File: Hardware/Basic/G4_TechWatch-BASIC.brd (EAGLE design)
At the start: 38 x 38 mm, 51 parts, among them J1 FTDI_DEVICESMD, SW3 SWITCH.MOM, SW4 SWITCH.MOM, SW5 SWITCH.MOM, U1 NRF52832_MODULE_MDBT42, U2 PCF8523

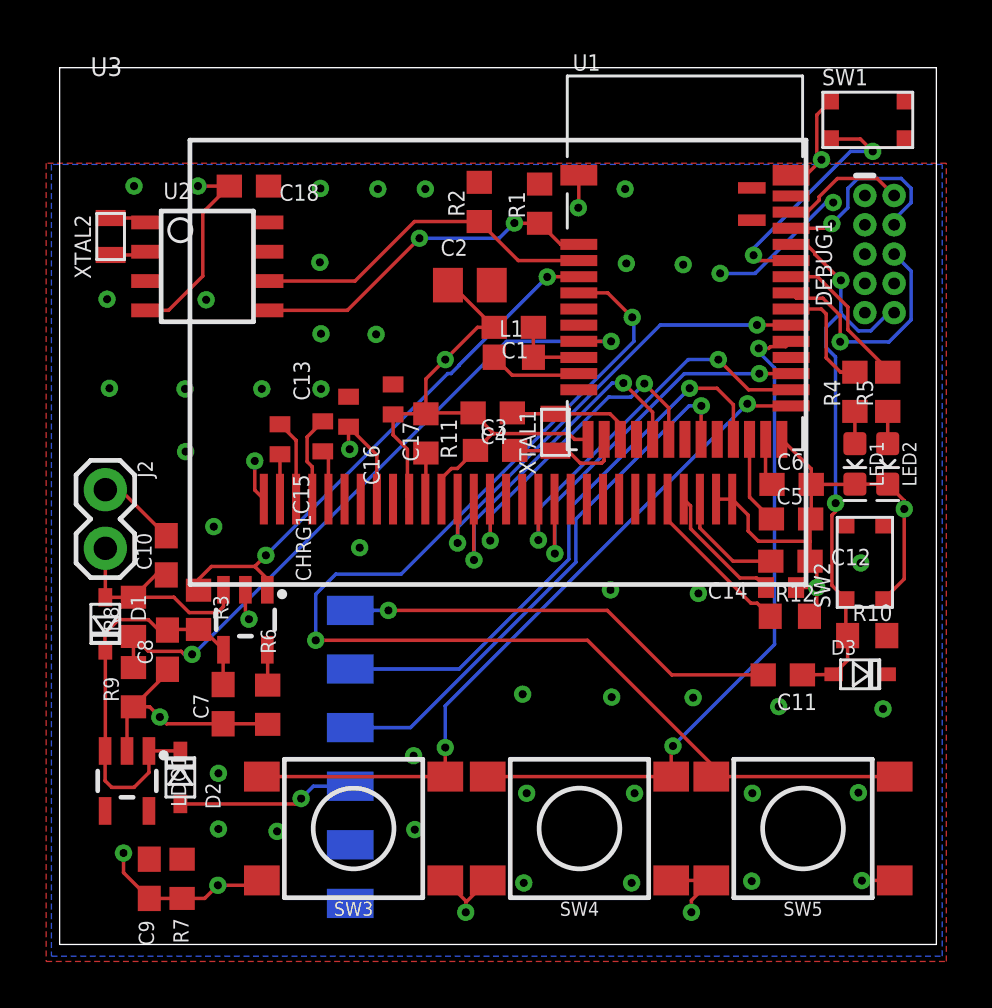
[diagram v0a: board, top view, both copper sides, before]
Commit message: Added Missing values, fixed silkscreen and OLED spacing
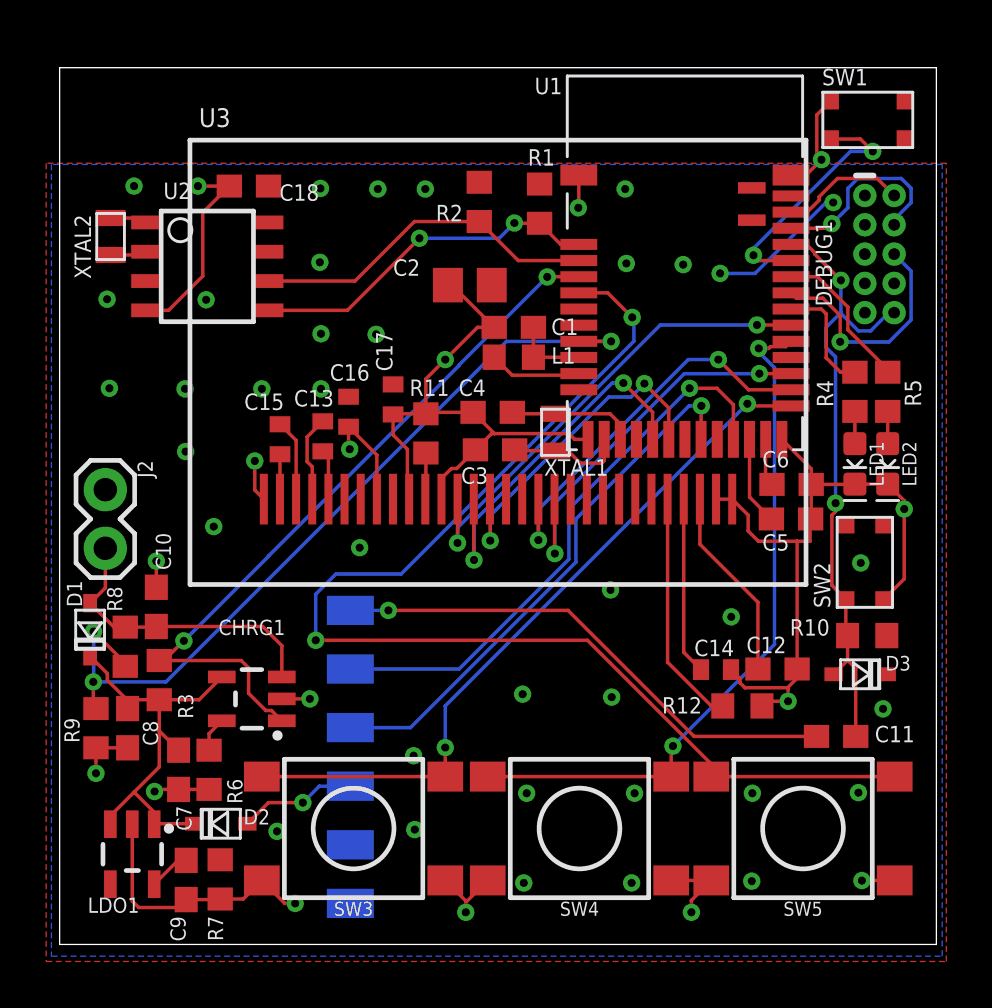
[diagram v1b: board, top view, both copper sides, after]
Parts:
- C3, C4: value (none) -> 12p
- R6: value (none) -> 10k
- moved C12 4.71 mm to (31.1, 11.9)
- moved C14 4.54 mm to (28.4, 11.9)
- moved R12 4.40 mm to (29.6, 10.3)
- moved C8 3.82 mm to (2.95, 9.37)
- moved R6 3.79 mm to (6.48, 7.57)
- moved C11 3.53 mm to (33.7, 9.02)
- moved R3 3.49 mm to (4.32, 11.5)
- moved CHRG1 3.44 mm to (8.33, 10.6), turned to 90 degrees
- moved C7 3.44 mm to (5.16, 7.57)
- moved LDO1 3.18 mm to (3.15, 3.91)
- moved D2 2.66 mm to (6.99, 5.23), turned to 180 degrees
- moved R9 2.41 mm to (1.57, 9.37)
- moved C10 2.28 mm to (4.19, 14.6)
- moved R7 1.65 mm to (6.96, 2.82)
- moved C9 1.60 mm to (5.49, 2.79)
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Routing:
- net CHRG.STAT: track 23.6 -> 32.1 mm
- net AIN7/BATT: track 29.4 -> 35.4 mm, vias 2 -> 3
- net N$13: track 4.92 -> 8.40 mm
- net DTR: track 19.1 -> 22.5 mm
- net N$2: track 7.08 -> 10.2 mm
- net VLIPO: track 10.2 -> 13.1 mm
- net GND: track 100.7 -> 103.3 mm, vias 54 -> 51
- net V_USB: track 7.68 -> 5.14 mm
- net RESET: track 25.3 -> 27.4 mm
- net N$15: track 5.73 -> 7.70 mm
- net 3.3V: track 6.18 -> 7.99 mm
